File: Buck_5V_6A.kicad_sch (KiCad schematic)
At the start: 10 parts, among them U2 TPSM63606RDLR

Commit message: Route the board and apply the prototype PCB checklist fixes
Routing
- Route power (pours, In2 power areas, vias) and all signals; add a
  Signal net class (0.15 mm width/clearance) for low-speed nets.
- J8 expansion header is now a 2x8 near the MCU.

Checklist red flags
- Crystal Y3 moved beside U1's OSC pins with C5/C6 outboard and no
  other signals under it.
- Vias untented by default (tented only under silkscreen); 15 mil
  test vias on key signals, recorded as DRC exclusions.
- ESD: U6/U7 split into four USBLC6-2SC6 (U6, U11, U7, U12), one per
  connector, with VBUS caps C50/C51; R12/R13 moved next to J13.
- GND test loop TP3 moved to the top edge beside J5.

Improvements
- Encoder connectors J7/J15 changed to keyed JST XH S4B side-entry.
- 43 passives/LEDs/FB2 moved from 0603 to 0805 (MPNs updated).
- Fifth M3 mounting hole H5 under J8.
- +3.3VA rerouted away from the crystal; acute track angles removed.
- Datasheet links filled in; silkscreen pin labels, pin maps, team
  names and date; reference labels cleared off pads and vias.
- Custom DRC rule for the J7/J15 silkscreen edge overhang.
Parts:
- C10: footprint Capacitor_SMD:C_0603_1608Metric -> Capacitor_SMD:C_0805_2012Metric; MPN GRM1885C1H8R2DA01D -> C0805C829C5GACTU; Manufacturer Murata -> KEMET
- C9: footprint Capacitor_SMD:C_0603_1608Metric -> Capacitor_SMD:C_0805_2012Metric; MPN GRM188R71C105KA12D -> GRM21BR71C105KA01L
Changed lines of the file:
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@@
 			)
 		)
-		(property "Footprint" "Capacitor_SMD:C_0603_1608Metric"
+		(property "Footprint" "Capacitor_SMD:C_0805_2012Metric"
 			(at 194.01 96.52 0)
 			(hide yes)
@@
 			)
 		)
-		(property "Datasheet" "https://search.murata.co.jp/Ceramy/image/img/A01X/G101/ENG/GRM1885C1H8R2DA01-01A.pdf"
+		(property "Datasheet" "https://content.kemet.com/datasheets/KEM_C1003_C0G_SMD.pdf"
 			(at 193.04 92.71 0)
 			(hide yes)
@@
 			)
 		)
-		(property "Manufacturer" "Murata"
-			(at 193.04 92.71 0)
-			(hide yes)
-			(show_name no)
-			(do_not_autoplace no)
-			(effects
-				(font
-					(size 1.27 1.27)
-				)
-			)
-		)
-		(property "MPN" "GRM1885C1H8R2DA01D"
+		(property "Manufacturer" "KEMET"
+			(at 193.04 92.71 0)
+			(hide yes)
+			(show_name no)
+			(do_not_autoplace no)
+			(effects
+				(font
+					(size 1.27 1.27)
+				)
+			)
+		)
+		(property "MPN" "C0805C829C5GACTU"
 			(at 193.04 92.71 0)
 			(hide yes)
@@
 			)
 		)
-		(property "Footprint" "Capacitor_SMD:C_0603_1608Metric"
+		(property "Footprint" "Capacitor_SMD:C_0805_2012Metric"
 			(at 103.84 114.3 0)
 			(hide yes)
@@
 			)
 		)
-		(property "Datasheet" "https://search.murata.co.jp/Ceramy/image/img/A01X/G101/ENG/GRM188R71C105KA12-01.pdf"
+		(property "Datasheet" "https://www.murata.com/en-us/products/productdetail?partno=GRM21BR71C105KA01%23"
 			(at 102.87 110.49 0)
 			(hide yes)
@@
 			)
 		)
-		(property "MPN" "GRM188R71C105KA12D"
-			(at 102.87 110.49 0)
-			(hide yes)
+		(property "MPN" "GRM21BR71C105KA01L"
+			(at 102.87 110.49 0)
+			(hide yes)

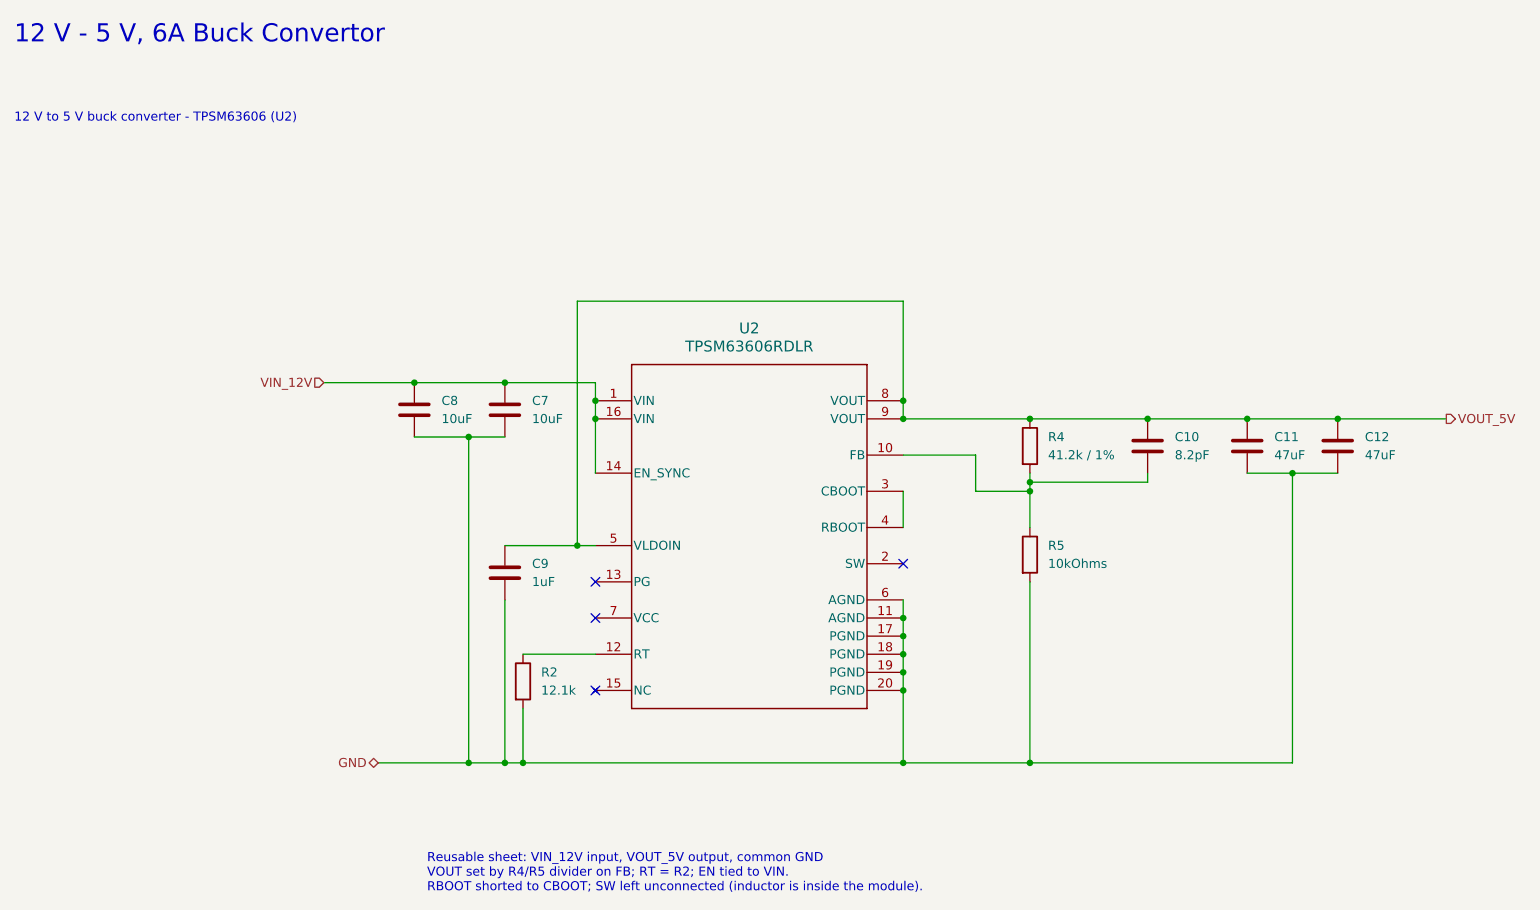
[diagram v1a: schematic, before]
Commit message: Replace out-of-stock buck converters with in-stock TI parts
TPSM63606 (U2, U5) and TPS54202 (U3) are out of stock at DigiKey.

- U2 (Pi 5 V) and U5 (AUX 5 V), 6 A: TPS56637RPAR with Wurth
  74439387033 3.3 uH, 2x 10 uF + 100 nF in, 47 uF out, 73.2k/10k
  feedback with 20k + 100 pF feed-forward, 100k PG pull-up. Values
  from TI WEBENCH (10-15 V in, 5 V 6 A); load-step sim 0.6->6 A
  stays within 4.91-5.06 V.
- U3 (+5V_SYS), 2 A: TPS54202HDDCR with TDK VLS6045EX-100M 10 uH,
  22 uF in, 47 uF out, 100k/13.7k + 68 pF, and a new 442k EN pull-up
  (R63) since the H version's EN is pulled down internally. Load-step
  sim 0.2->2 A stays within 4.72-5.21 V.
- New TPS56637 symbol, RPA0010A footprint (TI land pattern) and
  WE-XHMI-7070 footprint (Wurth land pattern).
- Layout follows the datasheet layout examples: TPS56637 Figure 34
  (VIN/Cin, inductor/Cout, AGND island, via arrays, inner-layer
  mirrors) and TPS54202H Figure 10-1 (SW through vias on an inner
  pour to the inductor, caps between GND and VIN copper).
- U5 moved below J8; PB7, PI_BOOT0, USART2_RX and the +5V_SYS feed
  rerouted around the new parts. New PG/EN resistors are R61-R63 to
  avoid the refs used on feat/battery-monitor-interior-light.
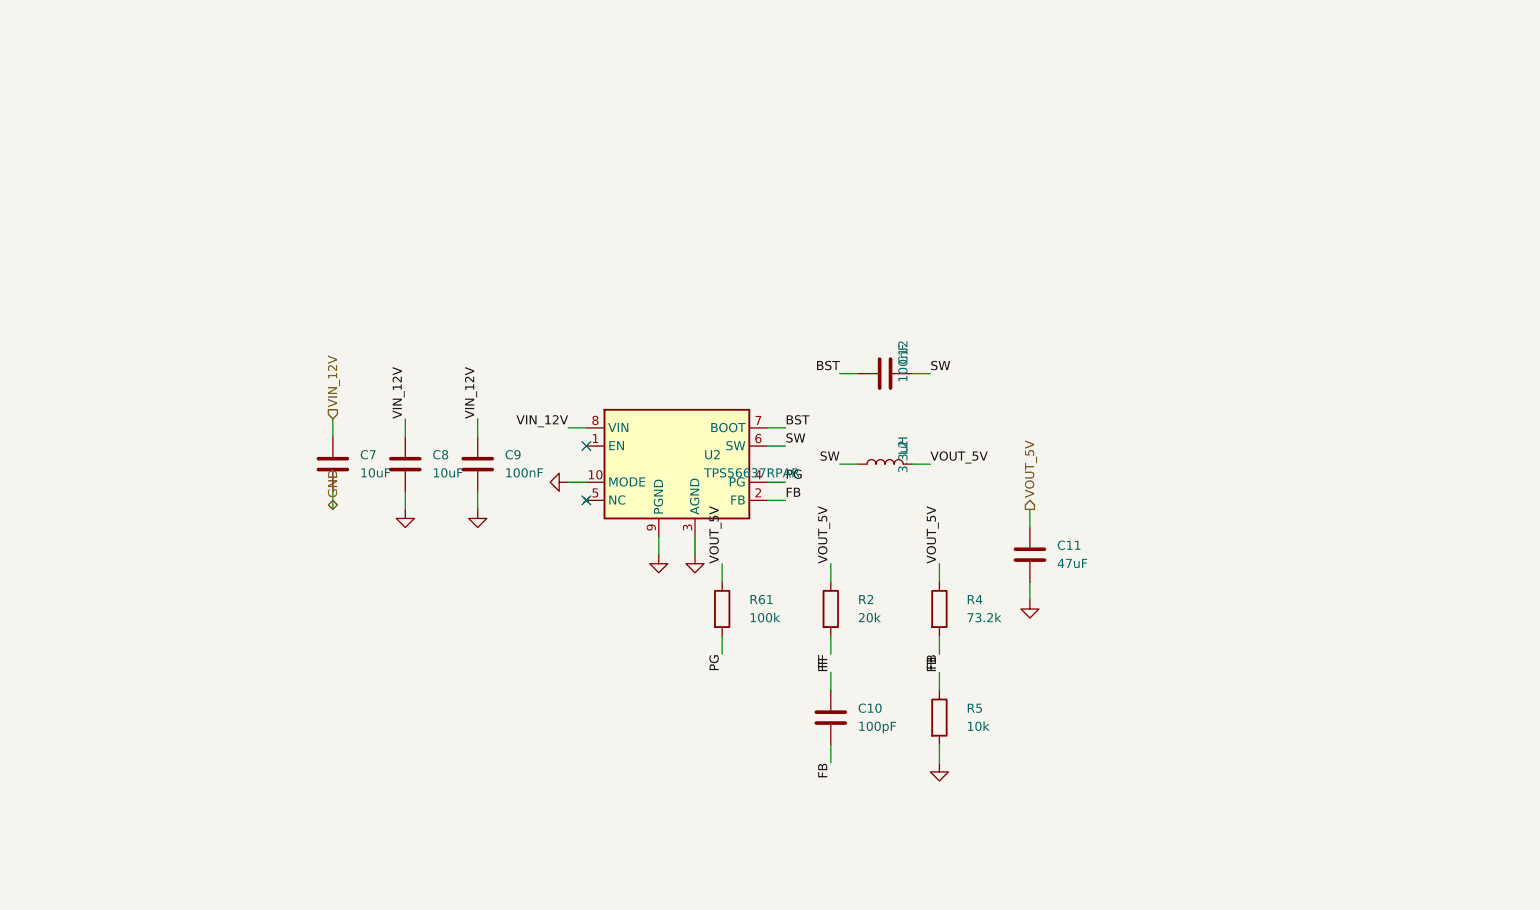
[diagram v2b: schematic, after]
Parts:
- added L2: 3.3uH, project_footprints:L_Wuerth_WE-XHMI-7070, symbol Device:L
- added R61: 100k, Resistor_SMD:R_0805_2012Metric, symbol Device:R
- C10: value 8.2pF -> 100pF; MPN C0805C829C5GACTU -> C0805C101J5GACTU; Specification 8.2pF / 50V C0G -> 100pF / 50V C0G (Cff)
- C11: footprint project_footprints:C_Murata_GRM32ER71A476ME15 -> Capacitor_SMD:C_1210_3225Metric; MPN GRM32ER71A476ME15L -> GRM32ER61C476KE15L; Specification 47uF / 10V X7R -> 47uF / 16V X5R 1210 (Cout)
- C12: value 47uF -> 100nF; footprint project_footprints:C_Murata_GRM32ER71A476ME15 -> Capacitor_SMD:C_0805_2012Metric; MPN GRM32ER71A476ME15L -> C0805C104K5RACTU; Manufacturer Murata -> KEMET; Specification 47uF / 10V X7R -> 100nF / 50V X7R (Cboot)
- C7, C8: footprint Capacitor_SMD:C_1210_3225Metric -> Capacitor_SMD:C_1206_3216Metric; MPN GRM32ER71H106KA12L -> GRM31CR71E106KA12L; Specification 10uF / 50V X7R -> 10uF / 25V X7R 1206 (Cin)
- C9: value 1uF -> 100nF; MPN GRM21BR71C105KA01L -> C0805C104K5RACTU; Manufacturer Murata -> KEMET; Specification 1uF / 16V X7R -> 100nF / 50V X7R (Cinx)
- R2: value 12.1k -> 20k; MPN (none) -> ERJ-6ENF2002V; Manufacturer (none) -> Panasonic; Specification (none) -> 20k 1% (Rff)
- R4: value 41.2k / 1% -> 73.2k; MPN (none) -> RC0805FR-0773K2L; Manufacturer (none) -> Yageo; Specification (none) -> 73.2k 1% (Rfbt)
- R5: value 10kOhms -> 10k; MPN (none) -> RC0805FR-0710KL; Manufacturer (none) -> Yageo; Specification (none) -> 10k 1% (Rfbb)
- U2: value TPSM63606RDLR -> TPS56637RPAR; footprint project_footprints:RDL0020A-MFG -> project_footprints:TI_RPA0010A_VQFN-HR-10_3x3mm; symbol TPSM63606RDLR:PTPSM63606RDLR -> TPS56637RPAR:TPS56637RPAR; Design Notes VOUT = VREF x (1 + R4/R5) with FB divider R4 41.2k / R5 10k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 -> (none); Key Specs VIN 3-36 V; VOUT 1-16 V adjustable; IOUT max 6 A; fsw 200 k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 -> (none); MPN TPSM63606RDLR -> TPS56637RPAR; Product Page https://www.ti.com/product/TPSM63606 -> (none); Specification (none) -> 6 A buck, 557 kHz, MODE=GND (Eco-mode); Used In Sheet Buck_5V_6A: 12 V in, +5V_PI net out -> (none)
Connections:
- net GND: now also U2.10 (MODE), U2.3 (AGND), U2.9 (PGND); no longer C12.2, R2.2, U2.11 (AGND), U2.17 (PGND), U2.18 (PGND), U2.19 (PGND), U2.20 (PGND), U2.6 (AGND)
- net VIN_12V: now also C9.1, U2.8 (VIN); no longer U2.1 (VIN), U2.14 (EN_SYNC), U2.16 (VIN)
- net VOUT_5V: now also R2.1, L2.2, R61.1; no longer C10.1, C12.1, C9.1, U2.5 (VLDOIN), U2.8 (VOUT), U2.9 (VOUT)
- net FB: now reaches C10.2, R4.2, R5.1
- net FB: now also U2.2 (FB); no longer U2.10 (FB)
- net PG: now reaches U2.4 (PG)
- net PG: now also R61.2; no longer U2.3 (CBOOT)
- net BST: now reaches U2.7 (BOOT)
- net BST: now also C12.1
- new net FF: C10.1, R2.2
- new net SW: C12.2, L2.1, U2.6 (SW)
- no-connect marks 4 -> 2
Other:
- note removed: "12 V - 5 V, 6A Buck Convertor"
- note removed: "12 V to 5 V buck converter - TPSM63606 (U2)"
- note removed: "Reusable sheet: VIN_12V input, VOUT_5V output, common GND VOUT set by R4/R5 divider on FB; RT = R2; EN tied to VIN. RBOOT shorted to CBOOT; SW left unconnected (inductor is inside the module)."
- moved on the sheet: C10, C11, C12, C7, C8, C9, R2, R4, R5

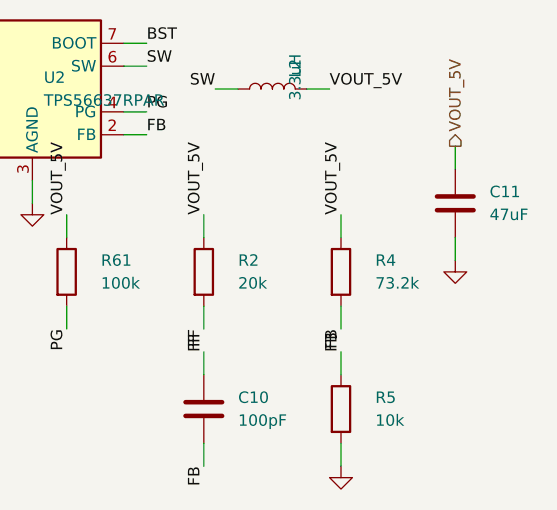
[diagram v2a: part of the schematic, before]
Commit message: Swap U13 to INA237 and set the Pi rail to 5.10 V
U13: INA228AIDGSR -> INA237AIDGSR. The INA228 is out of stock at TI,
LCSC and Mouser (next Mouser stock May 2027), and the INA238 is out
too. The INA237 has the same VSSOP-10 pinout, -0.3 V to 85 V common
mode, 0x40 address and +/-163.84 mV range, and Mouser stocks it. U13
keeps the Sensor_Energy:INA228 symbol (identical pins); only Value,
MPN, Datasheet and Description change, in the schematic and on the
board. It is 16-bit and has no CHARGE register, so firmware now
integrates current; the design-change doc has the new SHUNT_CAL
(819.2e6 x 4 mA x 1.5 mOhm = 4915) and accuracy budget.

R4: 73.2k -> 75k (RC0805FR-0775KL). +5V_PI = 0.6 V x (1 + 75/10) =
5.10 V instead of 4.99 V, back to the original design's ~5.1 V target
for harness drop at 5 A. R15 (AUX) stays 73.2k.

No connectivity, footprint or copper changes. delivery_robot_1.pdf,
system-ERC-report.txt and system-netlist.xml regenerated with KiCad
10.0.6 (the saved netlist was still from before the buck swap).

ERC: 0 errors, 0 warnings. DRC: 0 violations (4 excluded test vias),
0 unconnected, 0 parity issues.
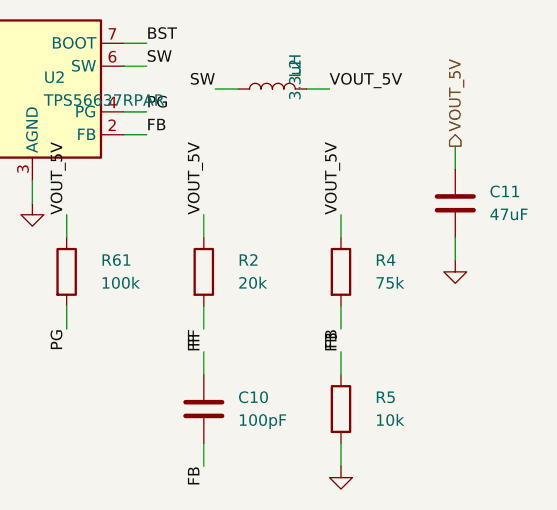
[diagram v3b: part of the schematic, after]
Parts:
- R4: value 73.2k -> 75k; MPN RC0805FR-0773K2L -> RC0805FR-0775KL; Specification 73.2k 1% (Rfbt) -> 75k 1% (Rfbt), sets +5V_PI to 5.10 V
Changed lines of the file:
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@@
 			(effects (font (size 1.27 1.27)) (justify left))
 		)
-		(property "Value" "73.2k"
+		(property "Value" "75k"
 			(at 167.64 116.84 0)
 			(show_name no)
@@
 			(effects (font (size 1.27 1.27)) (justify left))
 		)
-		(property "MPN" "RC0805FR-0773K2L"
+		(property "MPN" "RC0805FR-0775KL"
 			(at 163.83 120.65 0)
 			(hide yes)
@@
 			(effects (font (size 1.27 1.27)) (justify left))
 		)
-		(property "Specification" "73.2k 1% (Rfbt)"
+		(property "Specification" "75k 1% (Rfbt), sets +5V_PI to 5.10 V"
 			(at 163.83 120.65 0)
 			(hide yes)

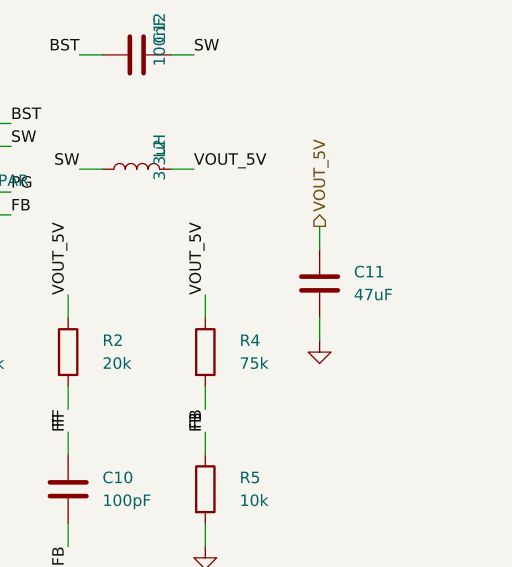
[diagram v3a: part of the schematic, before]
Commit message: Apply TA layout review: vias off pads, obtuse corners, buck layouts
- Move every via off its pad. The +3V3 vias at U6/U11/C34/C50 sit
  0.03-0.06 mm from the pad edge, without overlap, and are tented.
- Remove the remaining acute and right-angle track corners, including
  where tracks leave a pad, and straighten small jogs (R27 pin 2).
- U2/U5: add a second 47 uF output cap (C57, C58) to match the
  two-Cout datasheet layout, and add more PGND vias. F1 moves up 1 mm
  to make room for C57.
- U3: move C14 down 1 mm so the input cap GND pads have a via on each
  side.

DRC: 0 violations, 0 unconnected, 0 parity issues. ERC clean.
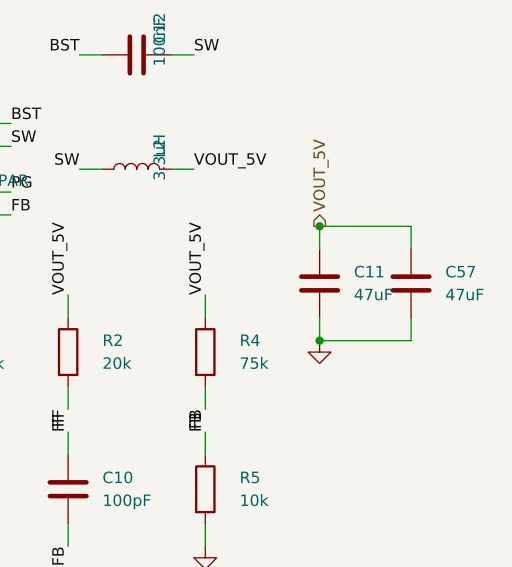
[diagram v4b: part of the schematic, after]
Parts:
- added C57: 47uF, Capacitor_SMD:C_1210_3225Metric, symbol Device:C
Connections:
- net GND: now also C57.2
- net VOUT_5V: now also C57.1
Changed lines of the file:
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@@
+		)
+	)
+	(symbol
+		(lib_id "Device:C")
+		(at 186.69 107.95 0)
+		(unit 1)
+		(body_style 1)
+		(exclude_from_sim no)
+		(in_bom yes)
+		(on_board yes)
+		(in_pos_files yes)
+		(dnp no)
+		(property "Reference" "C57"
+			(at 190.5 106.68 0)
+			(show_name no)
+			(do_not_autoplace no)
+			(effects (font (size 1.27 1.27)) (justify left))
+		)
+		(property "Value" "47uF"
+			(at 190.5 109.22 0)
+			(show_name no)
+			(do_not_autoplace no)
+			(effects (font (size 1.27 1.27)) (justify left))
+		)
+		(property "Footprint" "Capacitor_SMD:C_1210_3225Metric"
+			(at 186.69 113.03 0)
+			(hide yes)
+			(show_name no)
+			(do_not_autoplace no)
+			(effects (font (size 1.27 1.27)) (justify left))
+		)
+		(property "Datasheet" "https://search.murata.co.jp/Ceramy/image/img/A01X/G101/ENG/GRM32ER61C476KE15-01.pdf"
+			(at 186.69 113.03 0)
+			(hide yes)
+			(show_name no)
+			(do_not_autoplace no)
+			(effects (font (size 1.27 1.27)) (justify left))
+		)
+		(property "Description" "Unpolarized capacitor"
+			(at 186.69 113.03 0)
+			(hide yes)
+			(show_name no)
+			(do_not_autoplace no)
+			(effects (font (size 1.27 1.27)) (justify left))
+		)
+		(property "Manufacturer" "Murata"
+			(at 186.69 113.03 0)
+			(hide yes)
+			(show_name no)
+			(do_not_autoplace no)
+			(effects (font (size 1.27 1.27)) (justify left))
+		)
+		(property "MPN" "GRM32ER61C476KE15L"
+			(at 186.69 113.03 0)
+			(hide yes)
+			(show_name no)
+			(do_not_autoplace no)
+			(effects (font (size 1.27 1.27)) (justify left))
+		)
+		(property "Specification" "47uF / 16V X5R 1210 (Cout)"
+			(at 186.69 113.03 0)
+			(hide yes)
+			(show_name no)
+			(do_not_autoplace no)
+			(effects (font (size 1.27 1.27)) (justify left))
+		)
+		(pin "1")
+		(pin "2")
+		(instances
+			(project "delivery_robot_1"
+				(path "/30314d9c-15a8-4a77-8ae4-b5ba12ed5bc4/6703cd4e-ae4e-4732-91ad-54a19544ca3e"
+					(reference "C57")
+					(unit 1)
+				)
+			)
 		)
 	)
 	(wire
+		(pts (xy 186.69 104.14) (xy 186.69 101.6))
+		(stroke (width 0) (type default))
+	)
+	(wire
+		(pts (xy 186.69 101.6) (xy 176.53 101.6))
+		(stroke (width 0) (type default))
+	)
+	(wire
+		(pts (xy 186.69 111.76) (xy 186.69 114.3))
+		(stroke (width 0) (type default))
+	)
+	(wire
+		(pts (xy 186.69 114.3) (xy 176.53 114.3))
+		(stroke (width 0) (type default))
+	)
+	(junction
+		(at 176.53 101.6)
+		(diameter 0)
+		(color 0 0 0 0)
+	)
+	(junction
+		(at 176.53 114.3)
+		(diameter 0)
+		(color 0 0 0 0)
+	)
+	(wire
 		(pts (xy 176.53 104.14) (xy 176.53 101.6))
